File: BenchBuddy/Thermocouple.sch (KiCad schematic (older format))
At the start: 0 parts

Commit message: Week3 part 1
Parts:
- added C?: C, ~, symbol C
- added D?: ZENER, ~, symbol ZENER
- added R? (x7): R, ~, symbol R
- added U? (x4): LM324, symbol LM324
- added U? (x2): MCP3550-60-E/SN, SO8, symbol MCP3550-60-E/SN
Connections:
- net CS_N: now also U?.7 (~CS~)
- net MISO: now also U?.6 (SDO/~RDY~)
- net SCLK: now also U?.5 (SCK)
- net TC IN +: now also U?.3 (+)
- net TC IN -: now also U?.3 (+)
- new net: R?.1, R?.2, U?.1
- new net: R?.1, R?.2, U?.2 (-) (x3)
- new net: R?.2, R?.2, U?.1
- new net: R?.1, U?.1, U?.2 (Vin+)
- new net: R?.1, R?.2, U?.3 (+)
- new net: U?.1, U?.2 (-), U?.2 (Vin+)
- new net +12V: D?.2 (K), U?.3 (+), U?.4 (V+), U?.4 (V+), U?.4 (V+)
- new net -12V: U?.11 (V-), U?.11 (V-), U?.11 (V-)
- new net AGND: D?.1 (A), R?.1, U?.3 (Vin-), U?.3 (Vin-)
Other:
- note added: "16/24Bit ADC"
- note added: "Analog / TC Imput"
- note added: "General Temperature Sensor"
- note added: "Instrumentation Amp"

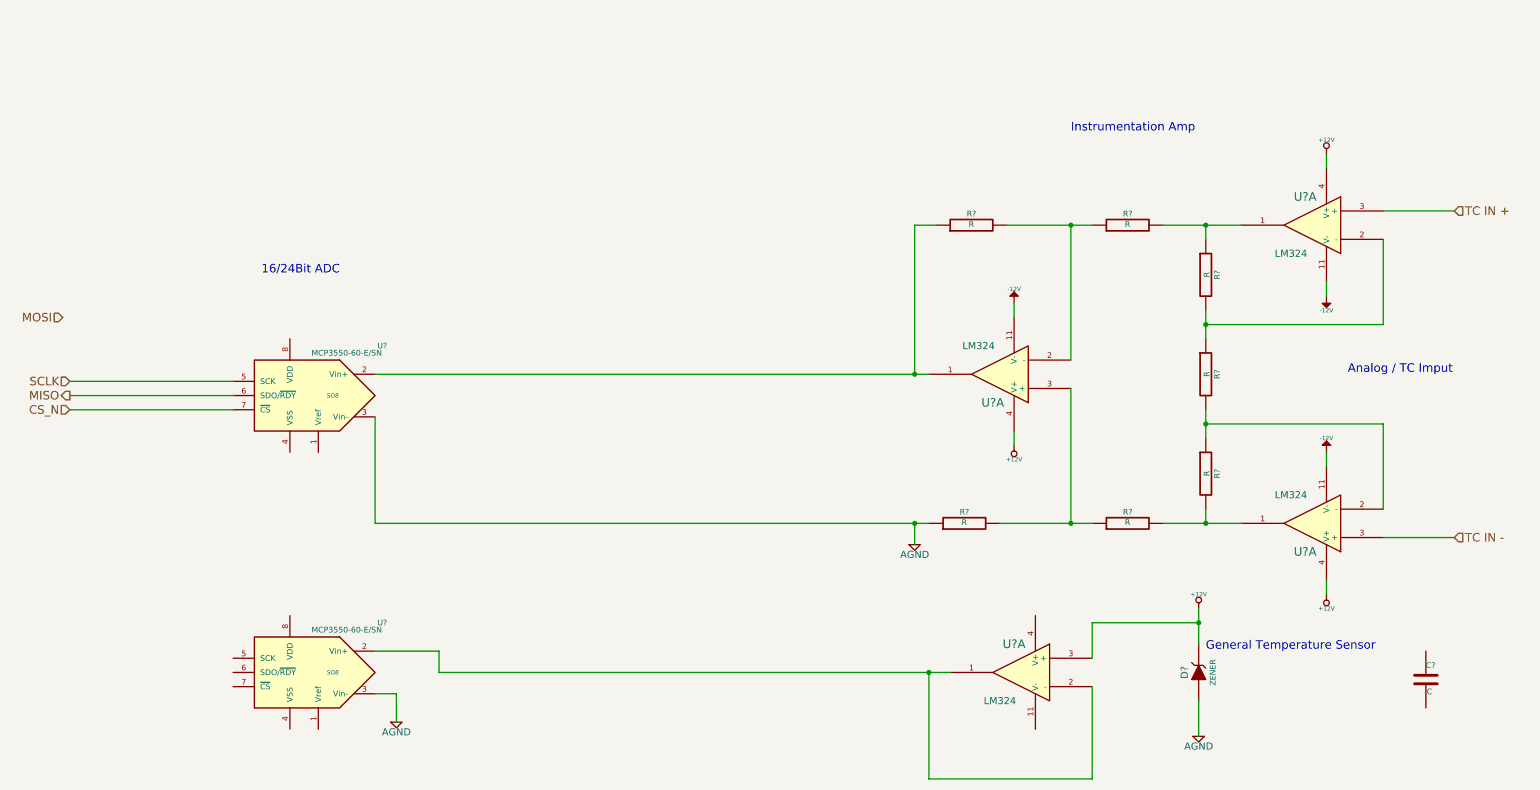
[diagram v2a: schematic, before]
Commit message: Colocação dos Componentes Relé
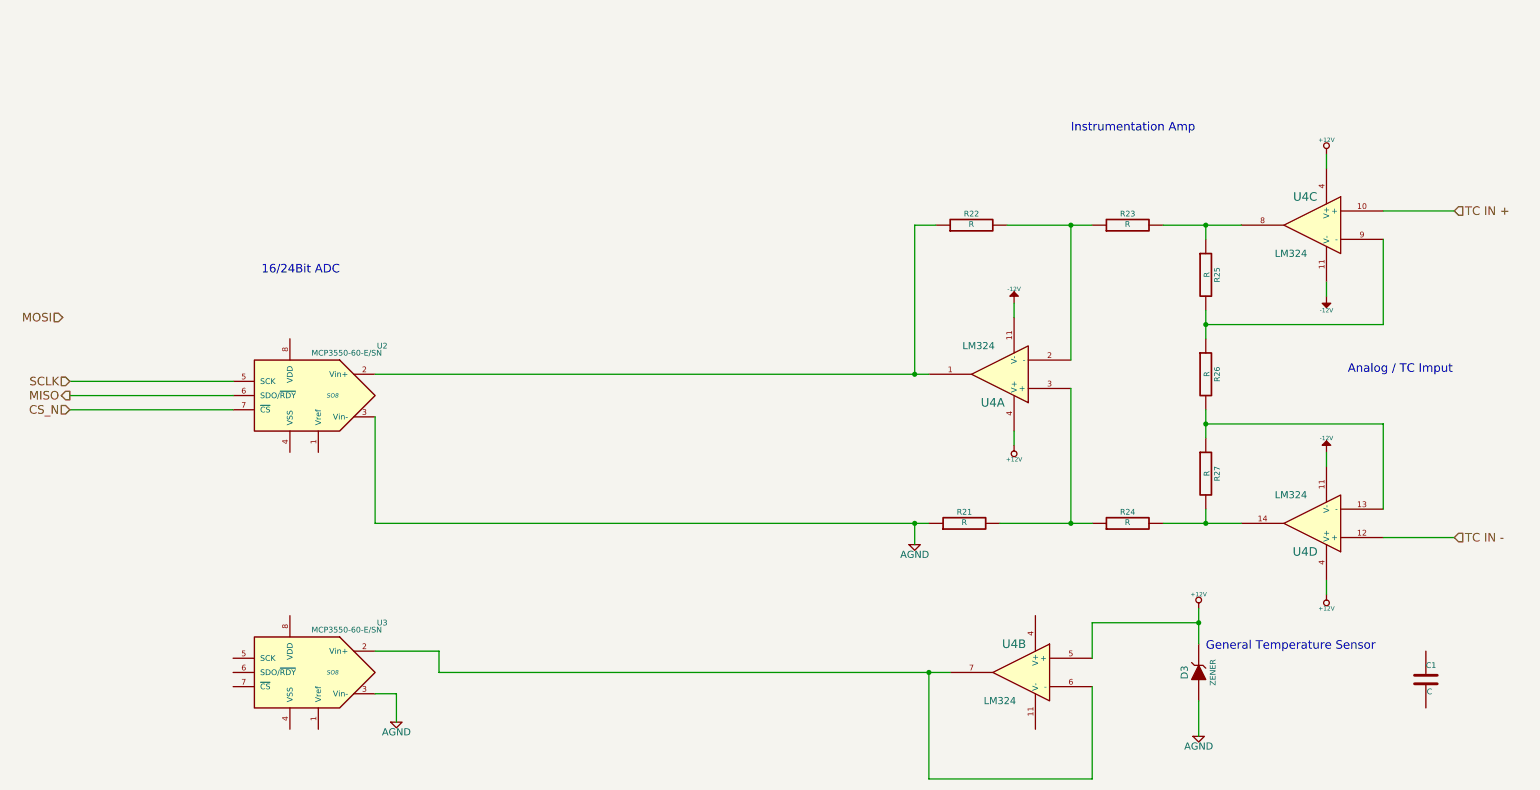
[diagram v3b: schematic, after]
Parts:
- gave numbers to parts that had none: 12
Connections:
- net +12V: now also U4.5 (+); no longer U4.3 (+)
- net TC IN +: now also U4.10 (+); no longer U4.3 (+)
- net TC IN -: now also U4.12 (+); no longer U4.3 (+)
- net at R23.2, R25.1: now also U4.8; no longer U4.1
- net at R25.2, R26.1: now also U4.9 (-); no longer U4.2 (-)
- net at R24.2, R27.2: now also U4.14; no longer U4.1
- net at R26.2, R27.1: now also U4.13 (-); no longer U4.2 (-)
- new net: U3.2 (Vin+), U4.6 (-), U4.7
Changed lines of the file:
@@
 Sheet 3 9
 Title ""
-Date "7 mar 2014"
+Date "9 mar 2014"
 Rev ""
 Comp ""
@@
 CS_N
 $Comp
-L LM324 U?
-U 1 1 5314F20B
+L LM324 U4
+U 3 1 5314F20B
 P 9650 3100
-F 0 "U?" H 9700 3300 60  0000 C CNN
+F 0 "U4" H 9700 3300 60  0000 C CNN
 F 1 "LM324" H 9800 2900 50  0000 C CNN
 F 2 "" H 9650 3100 60  0000 C CNN
 F 3 "" H 9650 3100 60  0000 C CNN
-	1    9650 3100
+	3    9650 3100
 	-1   0    0    -1
 $EndComp
 $Comp
-L LM324 U?
-U 1 1 5314F218
+L LM324 U4
+U 4 1 5314F218
 P 9650 5200
-F 0 "U?" H 9700 5400 60  0000 C CNN
+F 0 "U4" H 9700 5400 60  0000 C CNN
 F 1 "LM324" H 9800 5000 50  0000 C CNN
 F 2 "" H 9650 5200 60  0000 C CNN
 F 3 "" H 9650 5200 60  0000 C CNN
-	1    9650 5200
-	-1   0    0    1
-$EndComp
-$Comp
-L LM324 U?
+	4    9650 5200
+	-1   0    0    1
+$EndComp
+$Comp
+L LM324 U4
 U 1 1 5314F21E
 P 7450 4150
-F 0 "U?" H 7500 4350 60  0000 C CNN
+F 0 "U4" H 7500 4350 60  0000 C CNN
 F 1 "LM324" H 7600 3950 50  0000 C CNN
 F 2 "" H 7450 4150 60  0000 C CNN
@@
 $EndComp
 $Comp
-L LM324 U?
-U 1 1 5314F224
+L LM324 U4
+U 2 1 5314F224
 P 7600 6250
-F 0 "U?" H 7650 6450 60  0000 C CNN
+F 0 "U4" H 7650 6450 60  0000 C CNN
 F 1 "LM324" H 7750 6050 50  0000 C CNN
 F 2 "" H 7600 6250 60  0000 C CNN
 F 3 "" H 7600 6250 60  0000 C CNN
-	1    7600 6250
+	2    7600 6250
 	-1   0    0    -1
 $EndComp
 $Comp
-L C C?
+L C C1
 U 1 1 5314F261
 P 10450 6300
-F 0 "C?" H 10450 6400 40  0000 L CNN
+F 0 "C1" H 10450 6400 40  0000 L CNN
 F 1 "C" H 10456 6215 40  0000 L CNN
 F 2 "~" H 10488 6150 30  0000 C CNN
@@
 $EndComp
 $Comp
-L R R?
+L R R25
 U 1 1 5314F278
 P 8900 3450
-F 0 "R?" V 8980 3450 40  0000 C CNN
+F 0 "R25" V 8980 3450 40  0000 C CNN
 F 1 "R" V 8907 3451 40  0000 C CNN
 F 2 "~" V 8830 3450 30  0000 C CNN
@@
 $EndComp
 $Comp
-L R R?
+L R R26
 U 1 1 5314F2A3
 P 8900 4150
-F 0 "R?" V 8980 4150 40  0000 C CNN
+F 0 "R26" V 8980 4150 40  0000 C CNN
 F 1 "R" V 8907 4151 40  0000 C CNN
 F 2 "~" V 8830 4150 30  0000 C CNN
@@
 $EndComp
 $Comp
-L R R?
+L R R27
 U 1 1 5314F2A9
 P 8900 4850
-F 0 "R?" V 8980 4850 40  0000 C CNN
+F 0 "R27" V 8980 4850 40  0000 C CNN
 F 1 "R" V 8907 4851 40  0000 C CNN
 F 2 "~" V 8830 4850 30  0000 C CNN
@@
 $EndComp
 $Comp
-L R R?
+L R R23
 U 1 1 5314F358
 P 8350 3100
-F 0 "R?" V 8430 3100 40  0000 C CNN
+F 0 "R23" V 8430 3100 40  0000 C CNN
 F 1 "R" V 8357 3101 40  0000 C CNN
 F 2 "~" V 8280 3100 30  0000 C CNN
@@
 $EndComp
 $Comp
-L R R?
+L R R22
 U 1 1 5314F365
 P 7250 3100
-F 0 "R?" V 7330 3100 40  0000 C CNN
+F 0 "R22" V 7330 3100 40  0000 C CNN
 F 1 "R" V 7257 3101 40  0000 C CNN
 F 2 "~" V 7180 3100 30  0000 C CNN
@@
 $EndComp
 $Comp
-L R R?
+L R R21
 U 1 1 5314F3AC
 P 7200 5200
-F 0 "R?" V 7280 5200 40  0000 C CNN
+F 0 "R21" V 7280 5200 40  0000 C CNN
 F 1 "R" V 7207 5201 40  0000 C CNN
 F 2 "~" V 7130 5200 30  0000 C CNN
@@
 $EndComp
 $Comp
-L R R?
+L R R24
 U 1 1 5314F3B8
 P 8350 5200
-F 0 "R?" V 8430 5200 40  0000 C CNN
+F 0 "R24" V 8430 5200 40  0000 C CNN
 F 1 "R" V 8357 5201 40  0000 C CNN
 F 2 "~" V 8280 5200 30  0000 C CNN
@@
 $EndComp
 $Comp
-L -12V #PWR?
+L -12V #PWR5
 U 1 1 5314FD6C
 P 7550 3650
-F 0 "#PWR?" H 7550 3780 20  0001 C CNN
+F 0 "#PWR5" H 7550 3780 20  0001 C CNN
 F 1 "-12V" H 7550 3750 30  0000 C CNN
 F 2 "" H 7550 3650 60  0000 C CNN
@@
 $EndComp
 $Comp
-L -12V #PWR?
+L -12V #PWR11
 U 1 1 5314FD83
 P 9750 4700
-F 0 "#PWR?" H 9750 4830 20  0001 C CNN
+F 0 "#PWR11" H 9750 4830 20  0001 C CNN
 F 1 "-12V" H 9750 4800 30  0000 C CNN
 F 2 "" H 9750 4700 60  0000 C CNN
@@
 $EndComp
 $Comp
-L -12V #PWR?
+L -12V #PWR10
 U 1 1 5314FD93
 P 9750 3600
-F 0 "#PWR?" H 9750 3730 20  0001 C CNN
+F 0 "#PWR10" H 9750 3730 20  0001 C CNN
 F 1 "-12V" H 9750 3700 30  0000 C CNN
 F 2 "" H 9750 3600 60  0000 C CNN
@@
 $EndComp
 $Comp
-L +12V #PWR?
+L +12V #PWR6
 U 1 1 5314FDF6
 P 7550 4650
-F 0 "#PWR?" H 7550 4600 20  0001 C CNN
+F 0 "#PWR6" H 7550 4600 20  0001 C CNN
 F 1 "+12V" H 7550 4750 30  0000 C CNN
 F 2 "" H 7550 4650 60  0000 C CNN
@@
 $EndComp
 $Comp
-L +12V #PWR?
+L +12V #PWR12
 U 1 1 5314FE0D
 P 9750 5700
-F 0 "#PWR?" H 9750 5650 20  0001 C CNN
+F 0 "#PWR12" H 9750 5650 20  0001 C CNN
 F 1 "+12V" H 9750 5800 30  0000 C CNN
 F 2 "" H 9750 5700 60  0000 C CNN
@@
 $EndComp
 $Comp
-L +12V #PWR?
+L +12V #PWR9
 U 1 1 5314FE16
 P 9750 2600
-F 0 "#PWR?" H 9750 2550 20  0001 C CNN
+F 0 "#PWR9" H 9750 2550 20  0001 C CNN
 F 1 "+12V" H 9750 2700 30  0000 C CNN
 F 2 "" H 9750 2600 60  0000 C CNN
@@
 $EndComp
 $Comp
-L AGND #PWR?
+L AGND #PWR4
 U 1 1 5314FEC9
 P 6850 5350
-F 0 "#PWR?" H 6850 5350 40  0001 C CNN
+F 0 "#PWR4" H 6850 5350 40  0001 C CNN
 F 1 "AGND" H 6850 5280 50  0000 C CNN
 F 2 "" H 6850 5350 60  0000 C CNN
@@
 $EndComp
 $Comp
-L MCP3550-60-E/SN U?
+L MCP3550-60-E/SN U2
 U 1 1 5314FFF0
 P 2550 4300
-F 0 "U?" H 2000 4650 40  0000 C CNN
+F 0 "U2" H 2000 4650 40  0000 C CNN
 F 1 "MCP3550-60-E/SN" H 2250 4600 40  0000 C CNN
 F 2 "SO8" H 2350 4300 30  0000 C CIN
@@
 $EndComp
 $Comp
-L ZENER D?
+L ZENER D3
 U 1 1 5315032A
 P 8850 6250
-F 0 "D?" H 8850 6350 50  0000 C CNN
+F 0 "D3" H 8850 6350 50  0000 C CNN
 F 1 "ZENER" H 8850 6150 40  0000 C CNN
 F 2 "~" H 8850 6250 60  0000 C CNN
@@
 $EndComp
 $Comp
-L +12V #PWR?
+L +12V #PWR7
 U 1 1 53150346
 P 8850 5800
-F 0 "#PWR?" H 8850 5750 20  0001 C CNN
+F 0 "#PWR7" H 8850 5750 20  0001 C CNN
 F 1 "+12V" H 8850 5900 30  0000 C CNN
 F 2 "" H 8850 5800 60  0000 C CNN
@@
 $EndComp
 $Comp
-L AGND #PWR?
+L AGND #PWR8
 U 1 1 5315034C
 P 8850 6700
-F 0 "#PWR?" H 8850 6700 40  0001 C CNN
+F 0 "#PWR8" H 8850 6700 40  0001 C CNN
 F 1 "AGND" H 8850 6630 50  0000 C CNN
 F 2 "" H 8850 6700 60  0000 C CNN
@@
 	3500 6250 7100 6250
 $Comp
-L MCP3550-60-E/SN U?
+L MCP3550-60-E/SN U3
 U 1 1 53150429
 P 2550 6250
-F 0 "U?" H 2000 6600 40  0000 C CNN
+F 0 "U3" H 2000 6600 40  0000 C CNN
 F 1 "MCP3550-60-E/SN" H 2250 6550 40  0000 C CNN
 F 2 "SO8" H 2350 6250 30  0000 C CIN
@@
 Connection ~ 6950 6250
 $Comp
-L AGND #PWR?
+L AGND #PWR3
 U 1 1 53150461
 P 3200 6600
-F 0 "#PWR?" H 3200 6600 40  0001 C CNN
+F 0 "#PWR3" H 3200 6600 40  0001 C CNN
 F 1 "AGND" H 3200 6530 50  0000 C CNN
 F 2 "" H 3200 6600 60  0000 C CNN

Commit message: Pre layout
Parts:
- removed D3: ZENER, ~, symbol ZENER
- removed R26: R, ~, symbol R
- removed U2, U3: MCP3550-60-E/SN, SO8, symbol MCP3550-60-E/SN
- removed unit 2 of U4
- added C10, C6, C7, C8, C9: C, ~, symbol C
- added L5: INDUCTOR, SM0805, symbol INDUCTOR
- added P2: CONN_3X2, symbol CONN_3X2
- added P3: CONN_2, symbol CONN_2
- added R42, R43, R44: R, ~, symbol R
- added R50, R51: 0, ~, symbol R
- added U2: MCP3901, symbol MCP3901
- added U3: LMT84, symbol LMT84
- U4: value LM324 -> OPA4170
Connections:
- net AGND: now also C10.2, C6.2, C7.2, C8.2, C9.2, R50.1, R51.1, U2.11 (DGND), U2.8 (AGND), U3.1 (GND), U3.2 (GND), U3.5 (GND)
- net MISO: now also U2.19 (SDO)
- net MOSI: now also U2.20 (SDI)
- net SCLK: now also U2.18 (SCK)
- net at R25.2, U4.9 (-): now also P2.1, P2.3, P2.5
- net at R27.1, U4.13 (-): now also R42.2, R43.2, R44.2
- net CH0+: now reaches R22.1, U4.1
- net CH0+: now also C1.1, U2.4 (CH0+)
- net CH0-: now reaches C1.2
- net CH0-: now also R51.2, U2.5 (CH0-)
- net +12V renamed FE_V+
- net FE_V+: now also C10.1
- net -12V renamed FE_V-
- net FE_V-: now also C9.1
- new net: P3.1 (P1), U2.12 (MDAT0)
- new net: P3.2 (PM), U2.13 (MDAT1)
- new net: C6.1, L5.1, U2.2 (DVDD)
- new net: P2.2, R44.1
- new net: P2.4, R43.1
- new net: P2.6, R42.1
- new net +5V: C7.1, C8.1, U2.3 (AVDD), U3.4 (Vdd)
- new net CH1+: U2.7 (CH1+), U3.3 (OUT)
- new net CH1-: R50.2, U2.6 (CH1-)
- new net REF+: U2.9 (REFIN/OUT+)
- new net REF-: U2.10 (REFIN-)
- new net ~CS: U2.17 (~CS)
- new net ~DR: U2.14 (~DR)
- new net ~RESET: U2.1 (~RESET)
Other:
- note added: "Temp Sensor"
- note removed: "General Temperature Sensor"
- moved on the sheet: C1, R21, R22, R23, R24, R25, R27, U4A, U4C, U4D
